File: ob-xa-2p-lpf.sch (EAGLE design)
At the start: 56 parts, among them IC1 AS3320, IC3 TL082P

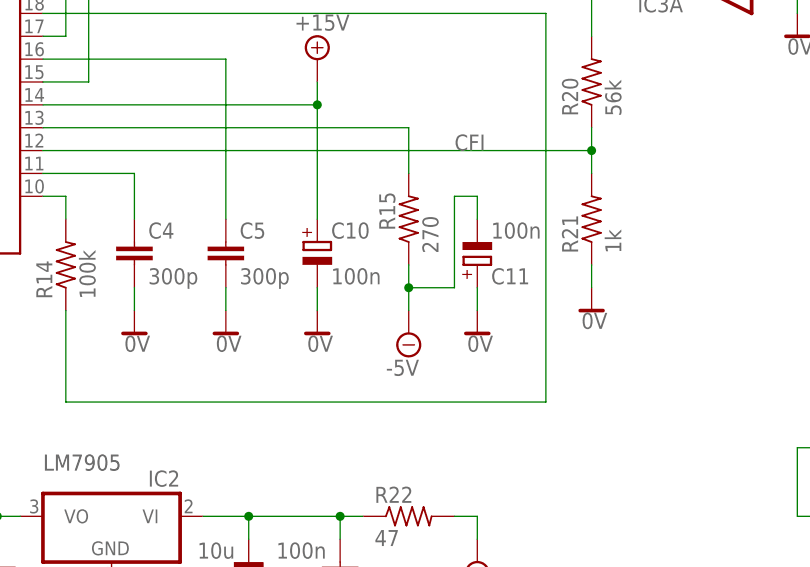
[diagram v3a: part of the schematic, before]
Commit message: drop -5V
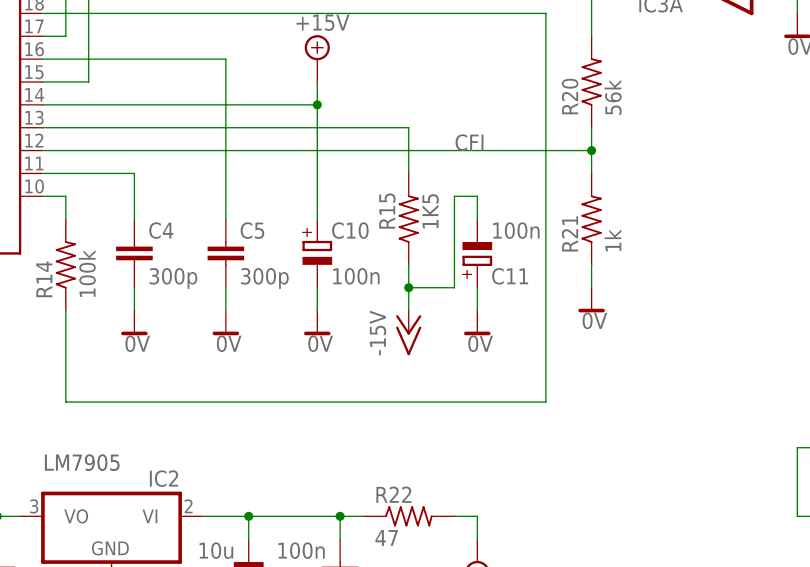
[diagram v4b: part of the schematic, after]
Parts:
- R15: value 270 -> 1K5
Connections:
- net -15V: now also C11.-, R15.1
- net -5V: no longer C11.-, R15.1
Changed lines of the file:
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@@
 <part name="V/OCT_ADJ" library="pot" library_urn="urn:adsk.eagle:library:331" deviceset="TRIM_US-" device="S63P" package3d_urn="urn:adsk.eagle:package:22705/1" value="10k"/>
 <part name="SUPPLY9" library="supply2" library_urn="urn:adsk.eagle:library:372" deviceset="+15V" device=""/>
-<part name="SUPPLY10" library="supply2" library_urn="urn:adsk.eagle:library:372" deviceset="-5V" device=""/>
 <part name="FREQ_CV_1" library="aarons_library" deviceset="OFFBOARD2JACKALT" device=""/>
 <part name="SUPPLY14" library="supply2" library_urn="urn:adsk.eagle:library:372" deviceset="0V" device=""/>
@@
 <part name="SUPPLY7" library="supply2" library_urn="urn:adsk.eagle:library:372" deviceset="0V" device=""/>
 <part name="R11" library="rcl" library_urn="urn:adsk.eagle:library:334" deviceset="R-US_" device="0207/10" package3d_urn="urn:adsk.eagle:package:23491/2" value="100k"/>
-<part name="R15" library="rcl" library_urn="urn:adsk.eagle:library:334" deviceset="R-US_" device="0207/10" package3d_urn="urn:adsk.eagle:package:23491/2" value="270"/>
+<part name="R15" library="rcl" library_urn="urn:adsk.eagle:library:334" deviceset="R-US_" device="0207/10" package3d_urn="urn:adsk.eagle:package:23491/2" value="1K5"/>
 <part name="C4" library="rcl" library_urn="urn:adsk.eagle:library:334" deviceset="C-EU" device="050-025X075" package3d_urn="urn:adsk.eagle:package:23637/1" value="300p"/>
 <part name="C5" library="rcl" library_urn="urn:adsk.eagle:library:334" deviceset="C-EU" device="050-025X075" package3d_urn="urn:adsk.eagle:package:23637/1" value="300p"/>
@@
 <part name="RES" library="pot" library_urn="urn:adsk.eagle:library:331" deviceset="TRIM_US-" device="B64Y" package3d_urn="urn:adsk.eagle:package:22690/1" value="100k"/>
 <part name="P+1" library="supply1" library_urn="urn:adsk.eagle:library:371" deviceset="+15V" device=""/>
+<part name="P-1" library="supply1" library_urn="urn:adsk.eagle:library:371" deviceset="-15V" device=""/>
 </parts>
 <sheets>
@@
 <attribute name="VALUE" x="127" y="38.735" size="1.778" layer="96"/>
 </instance>
-<instance part="SUPPLY10" gate="-5V" x="139.7" y="5.08" smashed="yes">
-<attribute name="VALUE" x="137.16" y="0.381" size="1.778" layer="96"/>
-</instance>
 <instance part="FREQ_CV_1" gate="G$1" x="228.6" y="60.96" smashed="yes">
 <attribute name="NAME" x="224.79" y="64.008" size="1.778" layer="95"/>
@@
 <instance part="R15" gate="G$1" x="139.7" y="17.78" smashed="yes" rot="R90">
 <attribute name="NAME" x="138.2014" y="16.51" size="1.778" layer="95" rot="R90"/>
-<attribute name="VALUE" x="143.002" y="13.97" size="1.778" layer="96" rot="R90"/>
+<attribute name="VALUE" x="143.002" y="16.51" size="1.778" layer="96" rot="R90"/>
 </instance>
 <instance part="C4" gate="G$1" x="109.22" y="15.24" smashed="yes">
@@
 <instance part="P+1" gate="1" x="53.34" y="15.24" smashed="yes">
 <attribute name="VALUE" x="50.8" y="10.16" size="1.778" layer="96" rot="R90"/>
+</instance>
+<instance part="P-1" gate="1" x="139.7" y="5.08" smashed="yes">
+<attribute name="VALUE" x="137.16" y="2.54" size="1.778" layer="96" rot="R90"/>
 </instance>
 </instances>
@@
 <net name="-5V" class="0">
 <segment>
-<pinref part="SUPPLY10" gate="-5V" pin="-5V"/>
-<pinref part="R15" gate="G$1" pin="1"/>
-<wire x1="139.7" y1="7.62" x2="139.7" y2="10.16" width="0.1524" layer="91"/>
-<wire x1="139.7" y1="10.16" x2="139.7" y2="12.7" width="0.1524" layer="91"/>
-<wire x1="139.7" y1="10.16" x2="144.78" y2="10.16" width="0.1524" layer="91"/>
-<junction x="139.7" y="10.16"/>
-<wire x1="144.78" y1="10.16" x2="144.78" y2="20.32" width="0.1524" layer="91"/>
-<wire x1="144.78" y1="20.32" x2="147.32" y2="20.32" width="0.1524" layer="91"/>
-<pinref part="C11" gate="G$1" pin="-"/>
-<wire x1="147.32" y1="17.78" x2="147.32" y2="20.32" width="0.1524" layer="91"/>
-</segment>
-<segment>
 <pinref part="IC2" gate="A1" pin="VO"/>
 <wire x1="96.52" y1="-15.24" x2="93.98" y2="-15.24" width="0.1524" layer="91"/>
@@
 <wire x1="193.04" y1="15.24" x2="193.04" y2="17.78" width="0.1524" layer="91"/>
 </segment>
-</net>
+<segment>
+<pinref part="R15" gate="G$1" pin="1"/>
+<wire x1="139.7" y1="7.62" x2="139.7" y2="10.16" width="0.1524" layer="91"/>
+<wire x1="139.7" y1="10.16" x2="139.7" y2="12.7" width="0.1524" layer="91"/>
+<wire x1="139.7" y1="10.16" x2="144.78" y2="10.16" width="0.1524" layer="91"/>
+<junction x="139.7" y="10.16"/>
+<wire x1="144.78" y1="10.16" x2="144.78" y2="20.32" width="0.1524" layer="91"/>
+<wire x1="144.78" y1="20.32" x2="147.32" y2="20.32" width="0.1524" layer="91"/>
+<pinref part="C11" gate="G$1" pin="-"/>
+<wire x1="147.32" y1="17.78" x2="147.32" y2="20.32" width="0.1524" layer="91"/>
+<pinref part="P-1" gate="1" pin="-15V"/>
+</segment>
+</net>

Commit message: improve power
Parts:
- removed C7, C9: 100n, rcl:C-EU050-025X075
- removed C8: 10u, rcl:CPOL-EUE1.8-4
- removed IC2: (no value), linear:7905T
- removed R22: 47, rcl:R-US_0207/10
- added L1, L2: (no value), rcl:L-US0207/10
- renumbered R26 to CV2
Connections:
- removed net -5V: C9.2, IC2.VO
- removed net N$21: C7.2, C8.-, IC2.VI, R22.1
- new net N$29: L1.1, POWER_IN.1
- new net N$31: L2.1, POWER_IN.4
- net +15V: now also C15.1, IC3P.V+, L1.2; no longer POWER_IN.1
- net -15V: now also C14.2, IC3P.V-, L2.2; no longer POWER_IN.4, R22.2
- net 0V: no longer C7.1, C8.+, C9.1, IC2.GND
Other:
- note removed: "LM7905"
- note removed: "Note: output capacitance less than 7905 datasheet."
- moved on the sheet: C10, C11, C12, C13, C14, C15, C5, R15, RES

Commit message: layout CV
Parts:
- renumbered R27 to FINE, R28 to COARSE
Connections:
- net N$29 renamed +15V_IN
- net N$31 renamed -15V_IN
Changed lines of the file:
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@@
 </variantdefs>
 <classes>
-<class number="0" name="default" width="0" drill="0">
+<class number="0" name="default" width="0.762" drill="0">
 </class>
 </classes>
@@
 <part name="SUPPLY26" library="supply2" library_urn="urn:adsk.eagle:library:372" deviceset="0V" device=""/>
 <part name="CV2" library="pot" library_urn="urn:adsk.eagle:library:331" deviceset="TRIM_US-" device="B64Y" package3d_urn="urn:adsk.eagle:package:22690/1" value="100k"/>
-<part name="R27" library="pot" library_urn="urn:adsk.eagle:library:331" deviceset="TRIM_US-" device="B64Y" package3d_urn="urn:adsk.eagle:package:22690/1" value="100k"/>
-<part name="R28" library="pot" library_urn="urn:adsk.eagle:library:331" deviceset="TRIM_US-" device="B64Y" package3d_urn="urn:adsk.eagle:package:22690/1" value="100k"/>
+<part name="FINE" library="pot" library_urn="urn:adsk.eagle:library:331" deviceset="TRIM_US-" device="B64Y" package3d_urn="urn:adsk.eagle:package:22690/1" value="100k"/>
+<part name="COARSE" library="pot" library_urn="urn:adsk.eagle:library:331" deviceset="TRIM_US-" device="B64Y" package3d_urn="urn:adsk.eagle:package:22690/1" value="100k"/>
 <part name="SUPPLY27" library="supply2" library_urn="urn:adsk.eagle:library:372" deviceset="0V" device=""/>
 <part name="SUPPLY28" library="supply2" library_urn="urn:adsk.eagle:library:372" deviceset="0V" device=""/>
@@
 <attribute name="VALUE" x="241.3" y="43.18" size="1.778" layer="96" rot="R270"/>
 </instance>
-<instance part="R27" gate="G$1" x="220.98" y="2.54" smashed="yes" rot="R180">
+<instance part="FINE" gate="G$1" x="220.98" y="2.54" smashed="yes" rot="R180">
 <attribute name="NAME" x="226.06" y="5.08" size="1.778" layer="95" rot="R270"/>
 <attribute name="VALUE" x="223.52" y="5.08" size="1.778" layer="96" rot="R270"/>
 </instance>
-<instance part="R28" gate="G$1" x="226.06" y="25.4" smashed="yes" rot="R180">
+<instance part="COARSE" gate="G$1" x="226.06" y="25.4" smashed="yes" rot="R180">
 <attribute name="NAME" x="231.14" y="27.94" size="1.778" layer="95" rot="R270"/>
 <attribute name="VALUE" x="228.6" y="27.94" size="1.778" layer="96" rot="R270"/>
@@
 </segment>
 <segment>
-<pinref part="R28" gate="G$1" pin="E"/>
+<pinref part="COARSE" gate="G$1" pin="E"/>
 <pinref part="SUPPLY28" gate="0V" pin="0V"/>
 <wire x1="226.06" y1="15.24" x2="226.06" y2="17.78" width="0.1524" layer="91"/>
 </segment>
 <segment>
-<pinref part="R27" gate="G$1" pin="E"/>
+<pinref part="FINE" gate="G$1" pin="E"/>
 <pinref part="SUPPLY29" gate="0V" pin="0V"/>
 <wire x1="220.98" y1="-7.62" x2="220.98" y2="-5.08" width="0.1524" layer="91"/>
@@
 </segment>
 <segment>
-<pinref part="R28" gate="G$1" pin="A"/>
+<pinref part="COARSE" gate="G$1" pin="A"/>
 <wire x1="226.06" y1="35.56" x2="226.06" y2="33.02" width="0.1524" layer="91"/>
 <pinref part="P+5" gate="1" pin="+15V"/>
 </segment>
 <segment>
-<pinref part="R27" gate="G$1" pin="A"/>
+<pinref part="FINE" gate="G$1" pin="A"/>
 <wire x1="220.98" y1="12.7" x2="220.98" y2="10.16" width="0.1524" layer="91"/>
 <pinref part="P+6" gate="1" pin="+15V"/>
@@
 <wire x1="205.74" y1="40.64" x2="218.44" y2="40.64" width="0.1524" layer="91"/>
 <wire x1="218.44" y1="40.64" x2="218.44" y2="25.4" width="0.1524" layer="91"/>
-<pinref part="R28" gate="G$1" pin="S"/>
+<pinref part="COARSE" gate="G$1" pin="S"/>
 <wire x1="218.44" y1="25.4" x2="220.98" y2="25.4" width="0.1524" layer="91"/>
 </segment>
@@
 <wire x1="205.74" y1="30.48" x2="210.82" y2="30.48" width="0.1524" layer="91"/>
 <wire x1="210.82" y1="30.48" x2="210.82" y2="2.54" width="0.1524" layer="91"/>
-<pinref part="R27" gate="G$1" pin="S"/>
+<pinref part="FINE" gate="G$1" pin="S"/>
 <wire x1="210.82" y1="2.54" x2="215.9" y2="2.54" width="0.1524" layer="91"/>
 </segment>
@@
 </segment>
 </net>
-<net name="N$29" class="0">
+<net name="+15V_IN" class="0">
 <segment>
 <pinref part="L1" gate="G$1" pin="1"/>
@@
 <pinref part="POWER_IN" gate="A" pin="1"/>
 <wire x1="-15.24" y1="0" x2="-20.32" y2="0" width="0.1524" layer="91"/>
-</segment>
-</net>
-<net name="N$31" class="0">
+<label x="-15.24" y="5.08" size="1.778" layer="95" rot="R90"/>
+</segment>
+</net>
+<net name="-15V_IN" class="0">
 <segment>
 <pinref part="L2" gate="G$1" pin="1"/>
@@
 <pinref part="POWER_IN" gate="A" pin="4"/>
 <wire x1="-15.24" y1="-7.62" x2="-20.32" y2="-7.62" width="0.1524" layer="91"/>
-</segment>
-</net>
+<label x="-15.24" y="-20.32" size="1.778" layer="95" rot="R90"/>
+</segment>
+</net>

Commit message: route everything
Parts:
- renumbered POWER_IN to PWR_IN
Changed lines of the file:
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@@
 </variantdefs>
 <classes>
-<class number="0" name="default" width="0.762" drill="0">
+<class number="0" name="default" width="0.4064" drill="0">
+</class>
+<class number="1" name="Power" width="0.762" drill="0">
 </class>
 </classes>
@@
 <part name="C13" library="rcl" library_urn="urn:adsk.eagle:library:334" deviceset="CPOL-EU" device="E1.8-4" package3d_urn="urn:adsk.eagle:package:23336/2" value="10u"/>
 <part name="SUPPLY20" library="supply2" library_urn="urn:adsk.eagle:library:372" deviceset="0V" device=""/>
-<part name="POWER_IN" library="pinhead" library_urn="urn:adsk.eagle:library:325" deviceset="PINHD-1X4" device="" package3d_urn="urn:adsk.eagle:package:22407/2"/>
+<part name="PWR_IN" library="pinhead" library_urn="urn:adsk.eagle:library:325" deviceset="PINHD-1X4" device="" package3d_urn="urn:adsk.eagle:package:22407/2"/>
 <part name="IC3" library="linear" library_urn="urn:adsk.eagle:library:262" deviceset="TL082" device="P" package3d_urn="urn:adsk.eagle:package:16409/2"/>
 <part name="SUPPLY23" library="supply2" library_urn="urn:adsk.eagle:library:372" deviceset="0V" device=""/>
@@
 <attribute name="VALUE" x="-6.477" y="-9.652" size="1.778" layer="96" rot="MR0"/>
 </instance>
-<instance part="POWER_IN" gate="A" x="-22.86" y="-5.08" smashed="yes" rot="MR0">
+<instance part="PWR_IN" gate="A" x="-22.86" y="-5.08" smashed="yes" rot="MR0">
 <attribute name="NAME" x="-16.51" y="3.175" size="1.778" layer="95" rot="MR0"/>
 <attribute name="VALUE" x="-16.51" y="-12.7" size="1.778" layer="96" rot="MR0"/>
@@
 </segment>
 <segment>
-<pinref part="POWER_IN" gate="A" pin="2"/>
+<pinref part="PWR_IN" gate="A" pin="2"/>
 <wire x1="-20.32" y1="-2.54" x2="-7.62" y2="-2.54" width="0.1524" layer="91"/>
 <wire x1="-7.62" y1="-2.54" x2="-7.62" y2="-5.08" width="0.1524" layer="91"/>
-<pinref part="POWER_IN" gate="A" pin="3"/>
+<pinref part="PWR_IN" gate="A" pin="3"/>
 <wire x1="-7.62" y1="-5.08" x2="-20.32" y2="-5.08" width="0.1524" layer="91"/>
 <pinref part="SUPPLY20" gate="0V" pin="0V"/>
@@
 </segment>
 </net>
-<net name="+15V" class="0">
+<net name="+15V" class="1">
 <segment>
 <pinref part="RES" gate="G$1" pin="E"/>
@@
 </segment>
 </net>
-<net name="-15V" class="0">
+<net name="-15V" class="1">
 <segment>
 <pinref part="SUPPLY25" gate="G$1" pin="-15V"/>
@@
 </segment>
 </net>
-<net name="+15V_IN" class="0">
+<net name="+15V_IN" class="1">
 <segment>
 <pinref part="L1" gate="G$1" pin="1"/>
 <wire x1="-12.7" y1="10.16" x2="-15.24" y2="10.16" width="0.1524" layer="91"/>
 <wire x1="-15.24" y1="10.16" x2="-15.24" y2="0" width="0.1524" layer="91"/>
-<pinref part="POWER_IN" gate="A" pin="1"/>
+<pinref part="PWR_IN" gate="A" pin="1"/>
 <wire x1="-15.24" y1="0" x2="-20.32" y2="0" width="0.1524" layer="91"/>
 <label x="-15.24" y="5.08" size="1.778" layer="95" rot="R90"/>
 </segment>
 </net>
-<net name="-15V_IN" class="0">
+<net name="-15V_IN" class="1">
 <segment>
 <pinref part="L2" gate="G$1" pin="1"/>
 <wire x1="-12.7" y1="-17.78" x2="-15.24" y2="-17.78" width="0.1524" layer="91"/>
 <wire x1="-15.24" y1="-17.78" x2="-15.24" y2="-7.62" width="0.1524" layer="91"/>
-<pinref part="POWER_IN" gate="A" pin="4"/>
+<pinref part="PWR_IN" gate="A" pin="4"/>
 <wire x1="-15.24" y1="-7.62" x2="-20.32" y2="-7.62" width="0.1524" layer="91"/>
 <label x="-15.24" y="-20.32" size="1.778" layer="95" rot="R90"/>

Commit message: minor cleanup. Draft2 rev
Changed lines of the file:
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@@
 <part name="R24" library="rcl" library_urn="urn:adsk.eagle:library:334" deviceset="R-US_" device="0207/10" package3d_urn="urn:adsk.eagle:package:23491/2" value="150k"/>
 <part name="R25" library="rcl" library_urn="urn:adsk.eagle:library:334" deviceset="R-US_" device="0207/10" package3d_urn="urn:adsk.eagle:package:23491/2" value="1M5"/>
-<part name="SUPPLY25" library="supply2" library_urn="urn:adsk.eagle:library:372" deviceset="-15V" device=""/>
 <part name="FREQ_CV_2" library="aarons_library" deviceset="OFFBOARD2JACKALT" device=""/>
 <part name="SUPPLY26" library="supply2" library_urn="urn:adsk.eagle:library:372" deviceset="0V" device=""/>
@@
 <part name="L1" library="rcl" library_urn="urn:adsk.eagle:library:334" deviceset="L-US" device="0207/10" package3d_urn="urn:adsk.eagle:package:23491/2"/>
 <part name="L2" library="rcl" library_urn="urn:adsk.eagle:library:334" deviceset="L-US" device="0207/10" package3d_urn="urn:adsk.eagle:package:23491/2"/>
+<part name="P-3" library="supply1" library_urn="urn:adsk.eagle:library:371" deviceset="-15V" device=""/>
 </parts>
 <sheets>
@@
 <attribute name="VALUE" x="204.47" y="33.782" size="1.778" layer="96" rot="R180"/>
 </instance>
-<instance part="SUPPLY25" gate="G$1" x="193.04" y="12.7" smashed="yes">
-<attribute name="VALUE" x="189.865" y="8.001" size="1.778" layer="96"/>
-</instance>
 <instance part="FREQ_CV_2" gate="G$1" x="248.92" y="48.26" smashed="yes">
 <attribute name="NAME" x="245.11" y="51.308" size="1.778" layer="95"/>
@@
 <attribute name="NAME" x="0" y="-19.05" size="1.778" layer="95" rot="R180"/>
 <attribute name="VALUE" x="0" y="-13.97" size="1.778" layer="96" rot="R180"/>
+</instance>
+<instance part="P-3" gate="1" x="193.04" y="12.7" smashed="yes">
+<attribute name="VALUE" x="190.5" y="10.16" size="1.778" layer="96" rot="R90"/>
 </instance>
 </instances>
@@
 <net name="-15V" class="1">
 <segment>
-<pinref part="SUPPLY25" gate="G$1" pin="-15V"/>
-<pinref part="R6" gate="G$1" pin="2"/>
-<wire x1="193.04" y1="15.24" x2="193.04" y2="17.78" width="0.1524" layer="91"/>
-</segment>
-<segment>
 <pinref part="R15" gate="G$1" pin="1"/>
 <wire x1="142.24" y1="7.62" x2="142.24" y2="10.16" width="0.1524" layer="91"/>
@@
 <junction x="12.7" y="-17.78"/>
 </segment>
-</net>
+<segment>
+<pinref part="R6" gate="G$1" pin="2"/>
+<wire x1="193.04" y1="15.24" x2="193.04" y2="17.78" width="0.1524" layer="91"/>
+<pinref part="P-3" gate="1" pin="-15V"/>
+</segment>
+</net>
